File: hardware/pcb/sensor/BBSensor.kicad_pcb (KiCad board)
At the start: 2 copper layers, 180 x 126 mm, 110 parts, among them J1 Earth, J501 AudioJack2_SwitchT, J502 AudioJack2_SwitchT, J503 AudioJack2_SwitchT, J504 AudioJack2_SwitchT, P1 Conn_WallPlug_Earth, SW1 SW_Push, U1 ESP8266-12E_NodeMCU_Lolin, U100 OPA2340, U101 OPA2340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

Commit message: feat: Split Display SPI converter from main PCB
split display
add new pcb

Issue #13
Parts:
- removed C301: 100n, Capacitor_THT:C_Disc_D3.4mm_W2.1mm_P2.50mm
- removed R301: 220, Resistor_THT:R_Axial_DIN0411_L9.9mm_D3.6mm_P12.70mm_Horizontal
- removed R302: 2k, Resistor_THT:R_Axial_DIN0411_L9.9mm_D3.6mm_P12.70mm_Horizontal
- removed U3: 74HC595, Package_DIP:DIP-16_W7.62mm_Socket
- removed U4: HD44780, Box_Header:Box_Header_Straight_2x08
- added J2: Display, Molex:Molex_KK256_Pin_Header_Straight_1x05, F.Cu at (67.9, 94.7)
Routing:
- net +5V: track 660.6 -> 512.6 mm
- net /Display/ENABLE: track 46.0 -> 0.00 mm
- net /Display/RS: track 43.5 -> 0.00 mm
- net GND: track 792.3 -> 753.2 mm
- net /Display/DB4: track 34.2 -> 0.00 mm
- net /Display/DB5: track 34.2 -> 0.00 mm
- net Net-(R301-Pad2): track 33.7 -> 0.00 mm
- net /Display/DB7: track 27.4 -> 0.00 mm
- net /Display/DB6: track 26.7 -> 0.00 mm
- net Net-(R302-Pad1): track 19.5 -> 0.00 mm
- net /Display/SPI5: track 39.9 -> 24.1 mm
- net /Analog/Digital/SPI3: track 75.1 -> 59.6 mm
- net Net-(TH4-Pad1): track 178.7 -> 177.4 mm
- net /Analog/Digital/SPI1: track 57.8 -> 58.8 mm

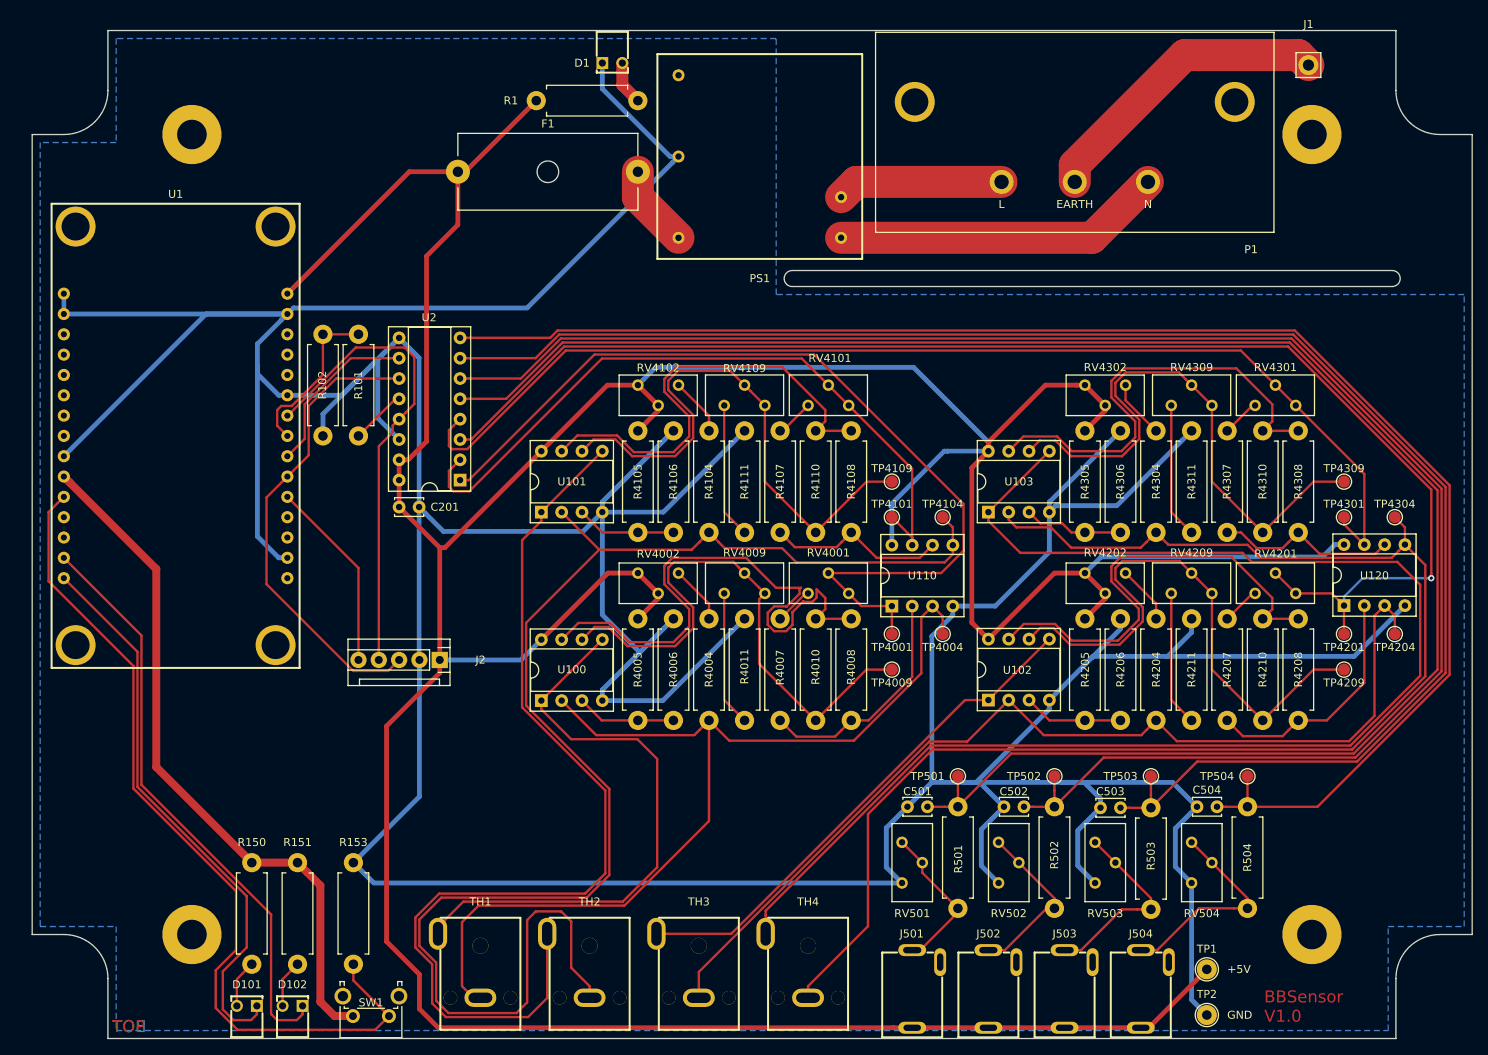
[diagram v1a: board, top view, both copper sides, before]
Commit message: feat: General PCB improvements
redo PCB, shrink it to 153 mm
generate PCB VRML

Issue #14
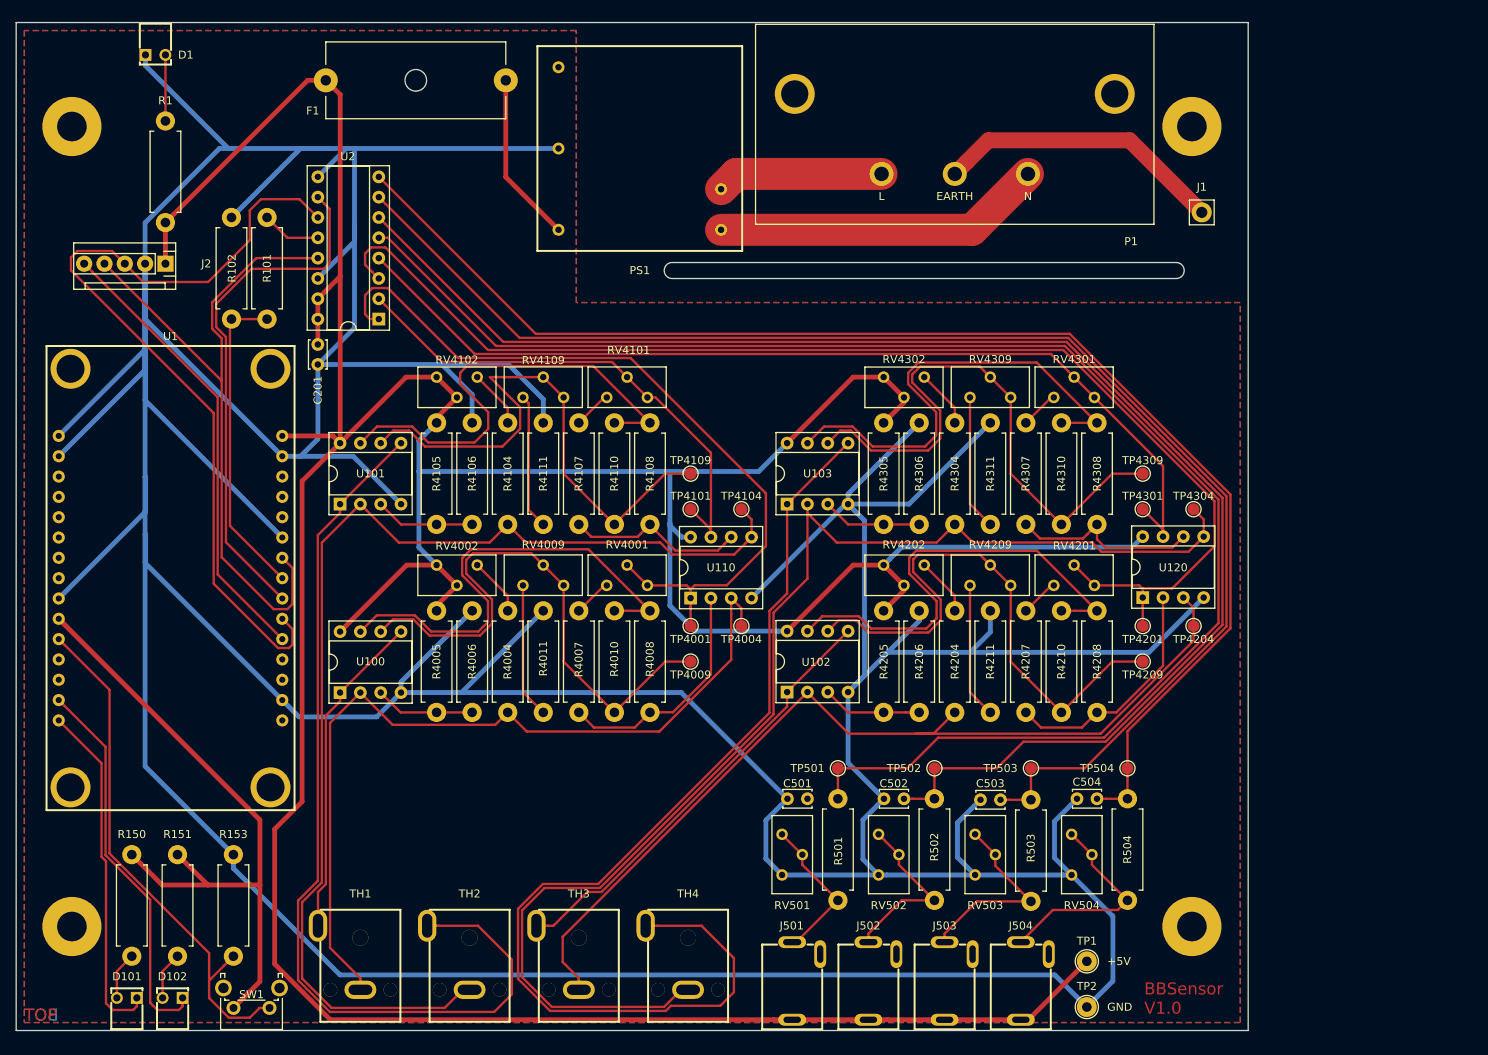
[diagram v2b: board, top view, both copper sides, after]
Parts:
- moved J2 60.2 mm to (33.7, 45.1)
- moved R1 59.1 mm to (33.7, 27.3), turned to 270 degrees
- moved D1 57.1 mm to (32.4, 15.1)
- moved R4211 25.2 mm to (136.8, 101.2)
- moved R4311 25.2 mm to (136.8, 77.7)
- moved RV4201 25.2 mm to (144.7, 85.4)
- moved RV4301 25.2 mm to (144.7, 61.9)
- moved RV4002 25.2 mm to (72.6, 82.8)
- moved RV4102 25.2 mm to (72.6, 59.3)
- moved U102 25.2 mm to (111.4, 98.7)
- moved U103 25.2 mm to (111.4, 75.2)
- moved R4004 25.2 mm to (76.4, 101.2)
- moved R4005 25.2 mm to (67.5, 101.2)
- moved R4006 25.2 mm to (72.0, 88.5)
- moved R4007 25.2 mm to (85.3, 88.5)
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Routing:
- net GND: track 753.2 -> 919.7 mm
- net /Analog/Digital/SPI1: track 58.8 -> 105.5 mm
- net /Analog/Digital/SPI4: track 21.6 -> 65.4 mm
- net Net-(TH4-Pad1): track 177.4 -> 134.7 mm
- net Net-(R153-Pad1): track 107.2 -> 66.0 mm
- net Net-(R4104-Pad1): track 184.5 -> 144.0 mm
- net /Analog/Digital/TEMP5: track 229.9 -> 192.9 mm
- net /Display/SPI5: track 24.1 -> 57.2 mm
- net Net-(TH1-Pad1): track 73.8 -> 41.1 mm
- net /Analog/Digital/TEMP6: track 218.4 -> 186.9 mm
- net /Analog/Digital/TEMP7: track 207.1 -> 177.3 mm
- net Net-(D101-Pad1): track 70.8 -> 43.3 mm
- net /Analog/Digital/SPI3: track 59.6 -> 86.7 mm
- net /Analog/Digital/TEMP8: track 195.5 -> 170.1 mm
- net Net-(D102-Pad1): track 73.4 -> 48.2 mm
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- added copper zone on F.Cu, net +5V
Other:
- board size 180 x 126 mm -> 154 x 126 mm

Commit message: feat: General PCB improvements
switch Power inlet

Issue #14
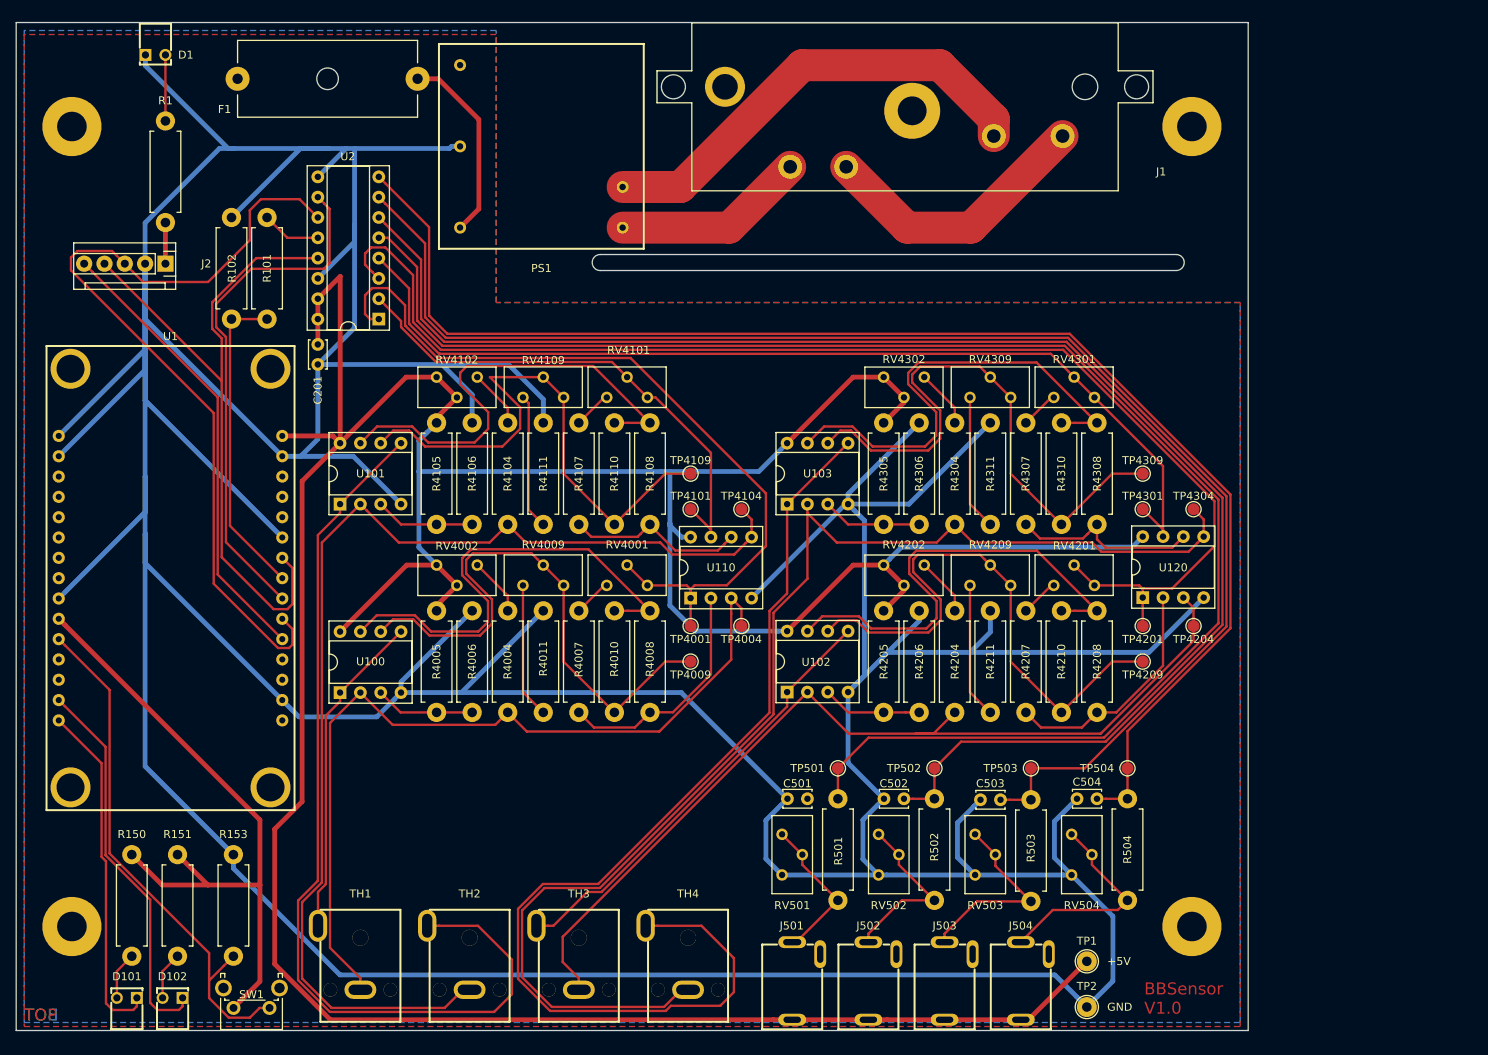
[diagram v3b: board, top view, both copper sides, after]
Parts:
- removed P1: Conn_WallPlug_Earth, Bulgin:PX0580PC
- J1: value Earth -> Schurter_CMF1; footprint Collection:Terminal_Pin_D1.3_L10.0_PL4.0 -> Schurter:CMF1
- moved J1 44.0 mm to (126.1, 15.0)
- moved PS1 12.3 mm to (80.6, 30.5)
- moved F1 11.0 mm to (42.7, 22.0)
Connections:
- PS1 pad 1: Net-(P1-Pad2) -> Net-(J1-Pad3)
- PS1 pad 2: Net-(P1-Pad1) -> Net-(J1-Pad1)
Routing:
- net +5V: track 502.3 -> 449.6 mm
- net Net-(P1-Pad2): track 41.3 -> 0.00 mm
- net Net-(J1-Pad2): track 0.00 -> 34.9 mm
- net Net-(J1-Pad3): track 0.00 -> 24.1 mm
- net Net-(J1-Pad1): track 36.3 -> 57.6 mm
- net Net-(P1-Pad1): track 20.8 -> 0.00 mm
- net GND: track 919.7 -> 907.5 mm
- net /Analog/Digital/TEMP8: track 170.1 -> 176.6 mm
- net /Analog/Digital/TEMP7: track 177.3 -> 182.7 mm
- net /Analog/Digital/TEMP6: track 186.9 -> 191.2 mm
- net /Analog/Digital/TEMP5: track 192.9 -> 196.8 mm
- net /Analog/Digital/TEMP3: track 154.7 -> 158.1 mm
- net Net-(F1-Pad2): track 21.4 -> 24.3 mm
- net /Analog/Digital/TEMP4: track 122.1 -> 124.7 mm
- net /Analog/Digital/TEMP1: track 97.5 -> 98.9 mm
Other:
- outline, holes or cut-outs redrawn
